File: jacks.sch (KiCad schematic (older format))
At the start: 73 parts, among them J601 PJ301BM, J602 PJ301BM, J603 PJ301BM, J604 PJ301BM, Q601 MMBT3904, Q602 MMBT3904, Q603 MMBT3904, Q604 MMBT3904, U601 MCP6004, U602 6N137

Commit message: work on schematic
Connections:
- net AREF_-10 renamed AREF_-10V

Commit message: work in progress
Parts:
- C601, C602, C603, C604: MFN (none) -> Murata; MFP (none) -> GRM1885C1H102FA01J
- C605, C606: value C -> 100n; MFN (none) -> Murata; MFP (none) -> GRM188R71E104JA01J
- R601, R605, R606, R610, R631: MFN (none) -> Panasonic; MFP (none) -> ERJ-3EKF1002V
- R602, R607: MFN (none) -> Panasonic; MFP (none) -> ERJ-3EKF4702V
- R603, R608, R623, R624, R629, R630: MFN (none) -> Panasonic; MFP (none) -> ERJ-3EKF1003V
- R604, R609: MFN (none) -> Panasonic; MFP (none) -> ERJ-3EKF3301V
- R611, R612, R613, R614, R615, R616, R617, R618: MFN (none) -> Panasonic; MFP (none) -> ERJ-3EKF1001V
- R619, R620, R625, R626: MFN (none) -> Panasonic; MFP (none) -> ERJ-3EKF3302V
- R621, R622, R627, R628: MFN (none) -> Panasonic; MFP (none) -> ERJ-3EKF2003V
- R632: MFN (none) -> Panasonic; MFP (none) -> ERJ-3EKF2200V
- R633, R634: MFN (none) -> Panasonic; MFP (none) -> ERJ-3EKF51R1V

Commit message: work in progress
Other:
- note added: "OPAMPS ARE REVERSED!"
- note added: "USE 5V DIRECTLY!"
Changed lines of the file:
@@
 NoConn ~ 7400 2450
 NoConn ~ 5900 2300
+Text Notes 1100 4250 0    197  ~ 39
+OPAMPS ARE REVERSED!
+Text Notes 4150 1050 0    197  ~ 39
+USE 5V DIRECTLY!
 $EndSCHEMATC

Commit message: more work on layout
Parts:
- removed R604, R609: 3.3k, Resistors_SMD:R_0603, symbol R
- R602, R607: value 4.7k -> 1k; MFP ERJ-3EKF4702V -> ERJ-3EKF1001V
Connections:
- net +12V: no longer R602.1, R607.1
- net GND: now also U601.10 (+), U601.12 (+), U601.3 (+), U601.5 (+); no longer U601.13 (-), U601.2 (-), U601.6 (-), U601.9 (-)
- net at C601.2, R619.2, R621.1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: now also U601.2 (-); no longer U601.3 (+)
- net at C603.2, R625.2, R627.1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: now also U601.9 (-); no longer U601.10 (+)
- net at C602.2, R620.2, R622.1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: now also U601.6 (-); no longer U601.5 (+)
- net at C604.2, R626.2, R628.1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: now also U601.13 (-); no longer U601.12 (+)
- new net +5V: R602.1, R607.1
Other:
- note removed: "OPAMPS ARE REVERSED!"
- note removed: "USE 5V DIRECTLY!"

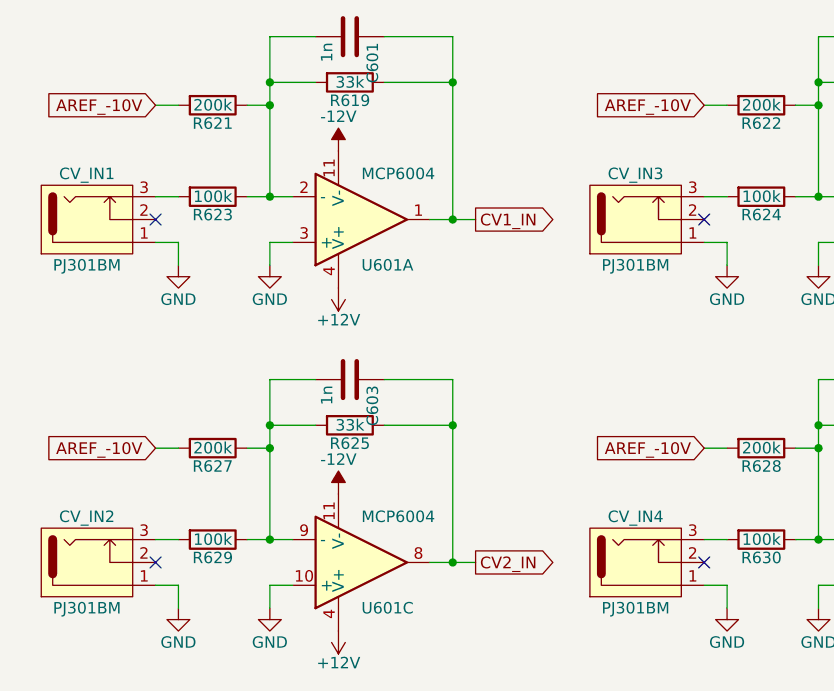
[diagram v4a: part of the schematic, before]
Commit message: renamed CV_INX to CVINX
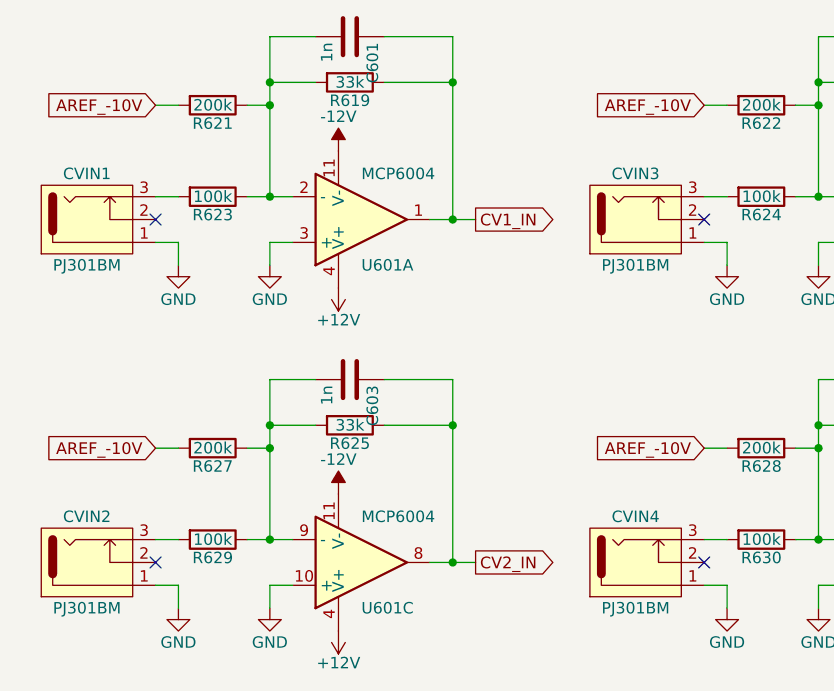
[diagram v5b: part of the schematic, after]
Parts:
- renumbered CV_IN1 to CVIN1, CV_IN2 to CVIN2, CV_IN3 to CVIN3, CV_IN4 to CVIN4
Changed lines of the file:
@@
 $EndComp
 $Comp
-L PJ301BM CV_IN1
+L PJ301BM CVIN1
 U 1 1 59DF34A9
 P 1000 5200
-F 0 "CV_IN1" H 800 5000 50  0000 C CNN
+F 0 "CVIN1" H 800 5000 50  0000 C CNN
 F 1 "PJ301BM" H 800 5400 50  0000 C CNN
 F 2 "w_connector:PJ301BM_OSH" H 1150 5300 50  0001 C CNN
@@
 $EndComp
 $Comp
-L PJ301BM CV_IN2
+L PJ301BM CVIN2
 U 1 1 59DFAD0D
 P 1000 6700
-F 0 "CV_IN2" H 800 6500 50  0000 C CNN
+F 0 "CVIN2" H 800 6500 50  0000 C CNN
 F 1 "PJ301BM" H 800 6900 50  0000 C CNN
 F 2 "w_connector:PJ301BM_OSH" H 1150 6800 50  0001 C CNN
@@
 $EndComp
 $Comp
-L PJ301BM CV_IN3
+L PJ301BM CVIN3
 U 1 1 59DFB737
 P 3400 5200
-F 0 "CV_IN3" H 3200 5000 50  0000 C CNN
+F 0 "CVIN3" H 3200 5000 50  0000 C CNN
 F 1 "PJ301BM" H 3200 5400 50  0000 C CNN
 F 2 "w_connector:PJ301BM_OSH" H 3550 5300 50  0001 C CNN
@@
 $EndComp
 $Comp
-L PJ301BM CV_IN4
+L PJ301BM CVIN4
 U 1 1 59DFB784
 P 3400 6700
-F 0 "CV_IN4" H 3200 6500 50  0000 C CNN
+F 0 "CVIN4" H 3200 6500 50  0000 C CNN
 F 1 "PJ301BM" H 3200 6900 50  0000 C CNN
 F 2 "w_connector:PJ301BM_OSH" H 3550 6800 50  0001 C CNN

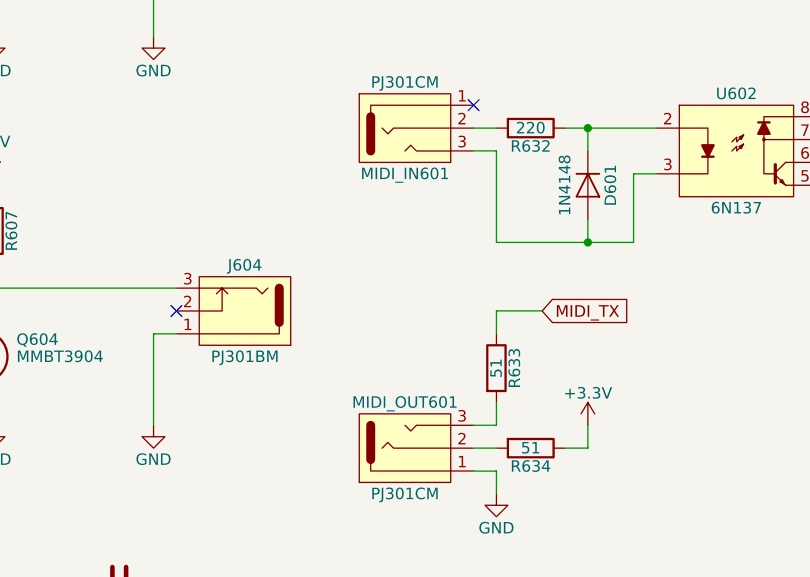
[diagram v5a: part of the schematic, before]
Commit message: renamed MIDIIN and MIDIOUT jacks
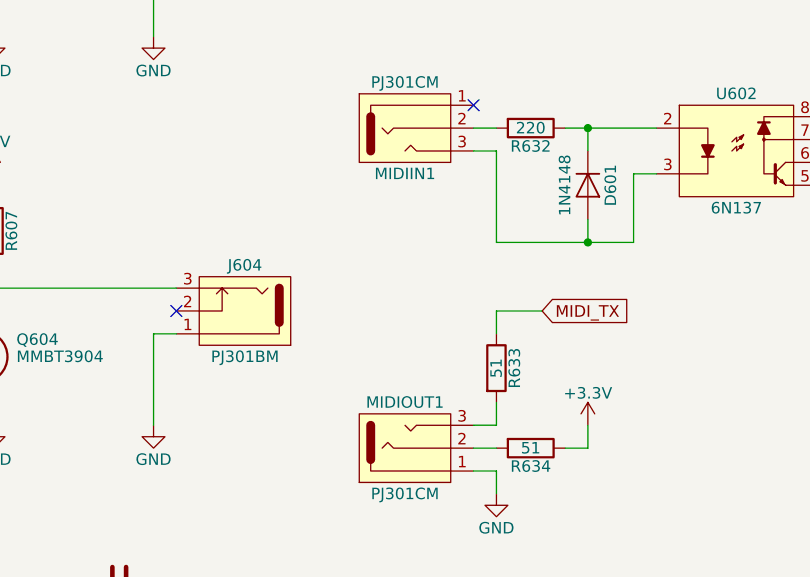
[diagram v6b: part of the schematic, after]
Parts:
- renumbered MIDI_IN601 to MIDIIN1, MIDI_OUT601 to MIDIOUT1
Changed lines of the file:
@@
 $EndComp
 $Comp
-L PJ301CM MIDI_IN601
+L PJ301CM MIDIIN1
 U 1 1 59DD452A
 P 5800 2400
-F 0 "MIDI_IN601" H 5600 2200 50  0000 C CNN
+F 0 "MIDIIN1" H 5600 2200 50  0000 C CNN
 F 1 "PJ301CM" H 5600 2600 50  0000 C CNN
 F 2 "w_connector:PJ301CM_OSH" H 5950 2500 50  0001 C CNN
@@
 $EndComp
 $Comp
-L PJ301CM MIDI_OUT601
+L PJ301CM MIDIOUT1
 U 1 1 59DD4899
 P 5800 3800
-F 0 "MIDI_OUT601" H 5600 3600 50  0000 C CNN
+F 0 "MIDIOUT1" H 5600 3600 50  0000 C CNN
 F 1 "PJ301CM" H 5600 4000 50  0000 C CNN
 F 2 "w_connector:PJ301CM_OSH" H 5950 3900 50  0001 C CNN

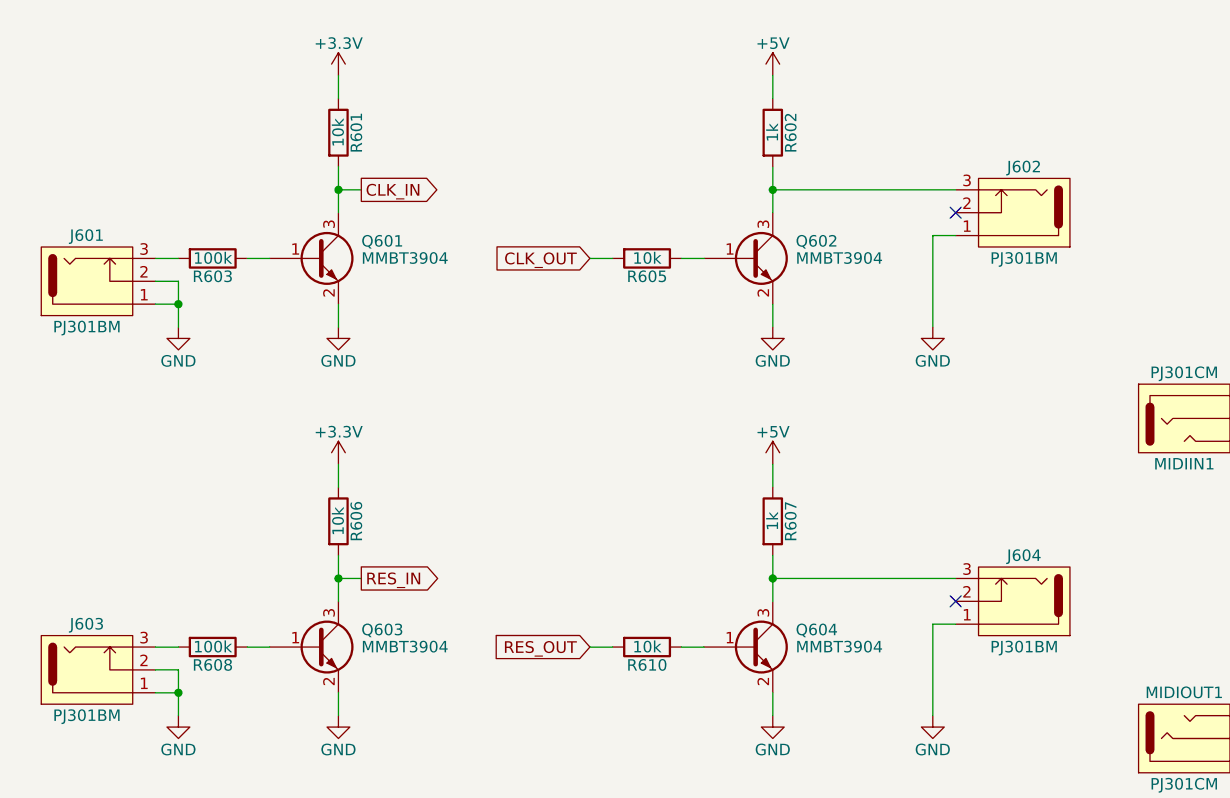
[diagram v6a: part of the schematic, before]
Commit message: renamed clock/reset input/output jacks
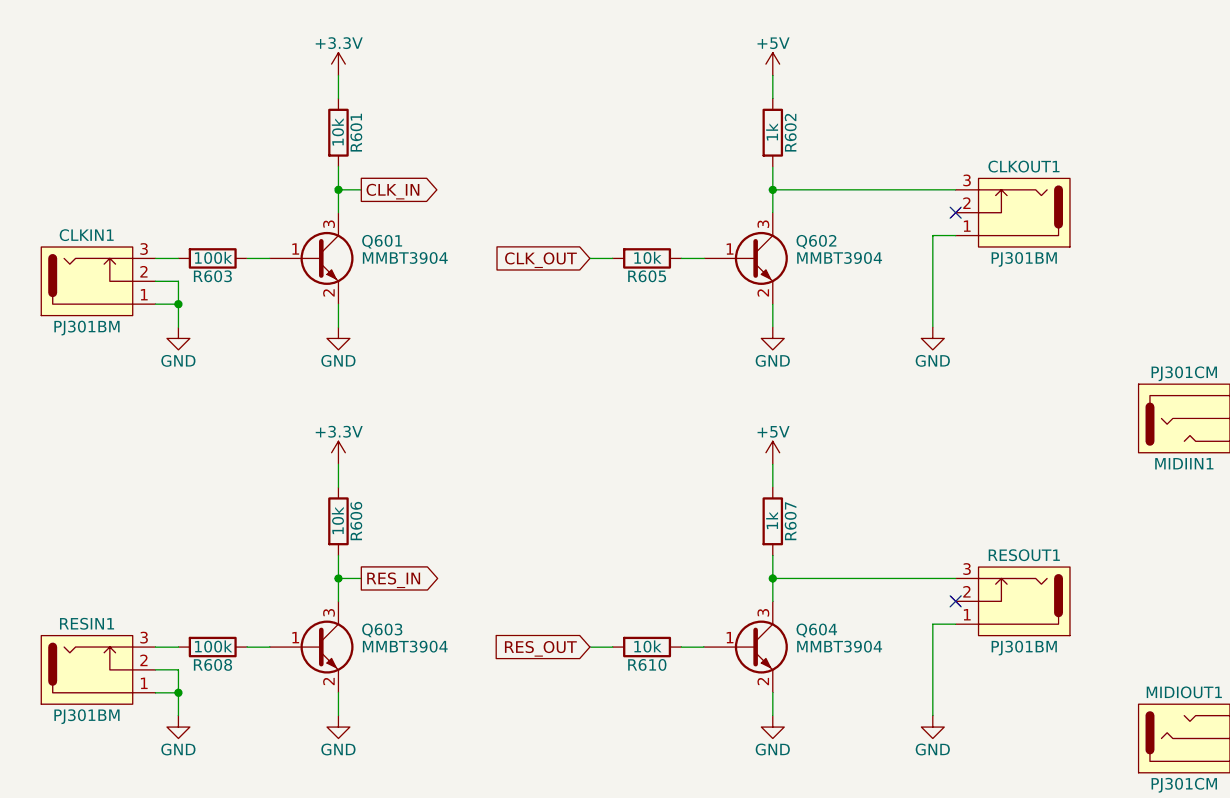
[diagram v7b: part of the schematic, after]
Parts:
- renumbered J601 to CLKIN1, J602 to CLKOUT1, J603 to RESIN1, J604 to RESOUT1
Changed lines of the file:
@@
 $EndComp
 $Comp
-L PJ301BM J601
+L PJ301BM CLKIN1
 U 1 1 59D9587D
 P 1000 1800
-F 0 "J601" H 800 1600 50  0000 C CNN
+F 0 "CLKIN1" H 800 1600 50  0000 C CNN
 F 1 "PJ301BM" H 800 2000 50  0000 C CNN
 F 2 "w_connector:PJ301BM_OSH" H 1150 1900 50  0001 C CNN
@@
 $EndComp
 $Comp
-L PJ301BM J603
+L PJ301BM RESIN1
 U 1 1 59D95DE7
 P 1000 3500
-F 0 "J603" H 800 3300 50  0000 C CNN
+F 0 "RESIN1" H 800 3300 50  0000 C CNN
 F 1 "PJ301BM" H 800 3700 50  0000 C CNN
 F 2 "w_connector:PJ301BM_OSH" H 1150 3600 50  0001 C CNN
@@
 $EndComp
 $Comp
-L PJ301BM J602
+L PJ301BM CLKOUT1
 U 1 1 59D96412
 P 4700 1500
-F 0 "J602" H 4500 1300 50  0000 C CNN
+F 0 "CLKOUT1" H 4500 1300 50  0000 C CNN
 F 1 "PJ301BM" H 4500 1700 50  0000 C CNN
 F 2 "w_connector:PJ301BM_OSH" H 4850 1600 50  0001 C CNN
@@
 $EndComp
 $Comp
-L PJ301BM J604
+L PJ301BM RESOUT1
 U 1 1 59D970A1
 P 4700 3200
-F 0 "J604" H 4500 3000 50  0000 C CNN
+F 0 "RESOUT1" H 4500 3000 50  0000 C CNN
 F 1 "PJ301BM" H 4500 3400 50  0000 C CNN
 F 2 "w_connector:PJ301BM_OSH" H 4850 3300 50  0001 C CNN

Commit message: redesign in progress
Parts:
- CLKIN1, CLKOUT1, CV1, CV2, CV3, CV4, CV5, CV6, CV7, CV8, CVIN1, CVIN2, CVIN3, CVIN4, GATE1, GATE2, GATE3, GATE4, GATE5, GATE6, GATE7, GATE8, RESIN1, RESOUT1: footprint w_connector:PJ301BM_OSH -> w_connector:PJ301BM
- MIDIIN1, MIDIOUT1: footprint w_connector:PJ301CM_OSH -> w_connector:PJ301CM
